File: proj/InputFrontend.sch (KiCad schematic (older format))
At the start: 0 parts

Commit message: Add frontend
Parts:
- added C?: 47u, IPC7351-Nominal:CAPC3216X70, symbol C-1206
- added C? (x12): 1n, IPC7351-Nominal:CAPC1005X55, symbol C-0402
- added C? (x6): 220n, IPC7351-Nominal:CAPC2012X70, symbol C-0805
- added MP?: SHIELD, symbol SHIELD
- added R? (x2): 49R9, IPC7351-Nominal:RESC1005X40, symbol R-0402
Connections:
- new net: C?.1, C?.1, R?.1, R?.2
- new net +5: C?.1, C?.1, C?.1, C?.1, C?.1, C?.1, C?.1, C?.1
- new net -5: C?.1, C?.1, C?.1, C?.1, C?.1, C?.1, C?.1, C?.1, C?.1
- new net Detector/OUT: R?.2
- new net GND: C?.2, C?.2, C?.2, C?.2, C?.2, C?.2, C?.2, C?.2, C?.2, C?.2, C?.2, C?.2, C?.2, C?.2, C?.2, C?.2, C?.2, C?.2, C?.2, MP?.1
- new net OUT: R?.1

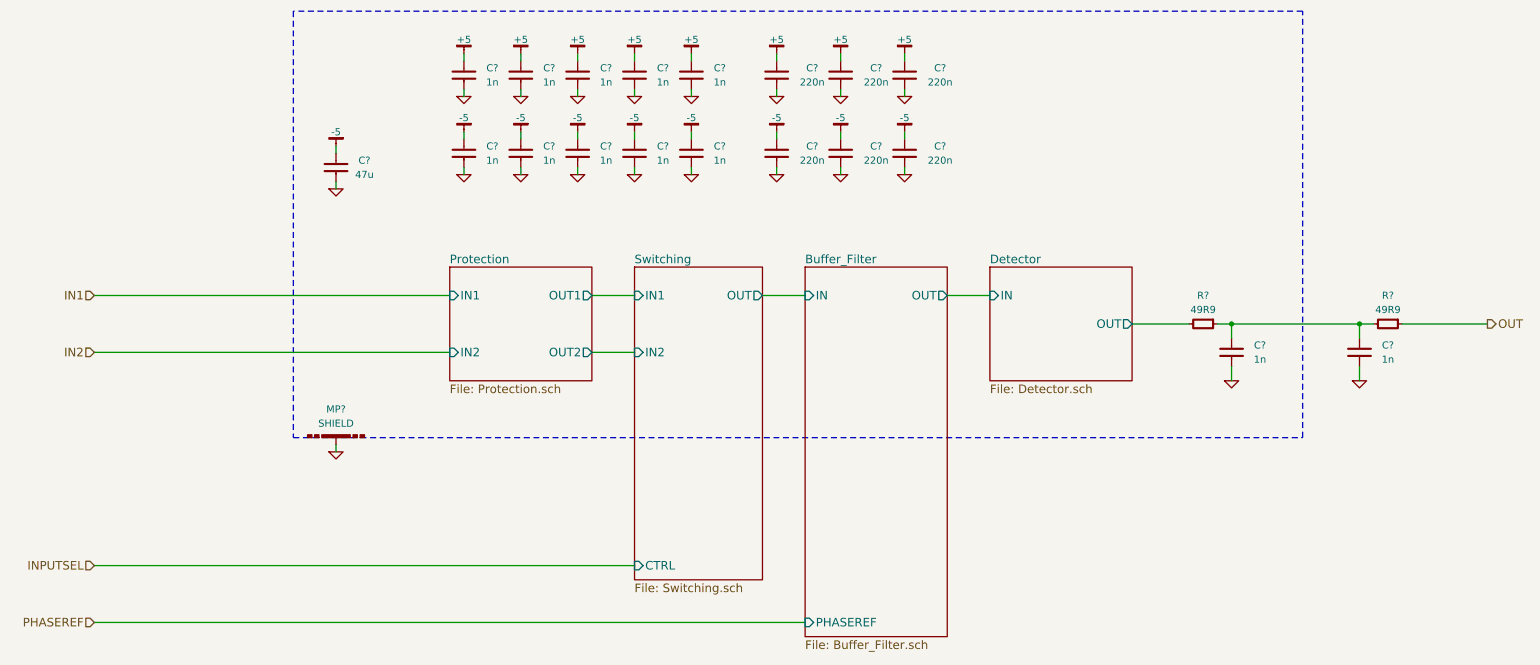
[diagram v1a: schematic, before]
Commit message: Add power input circuit
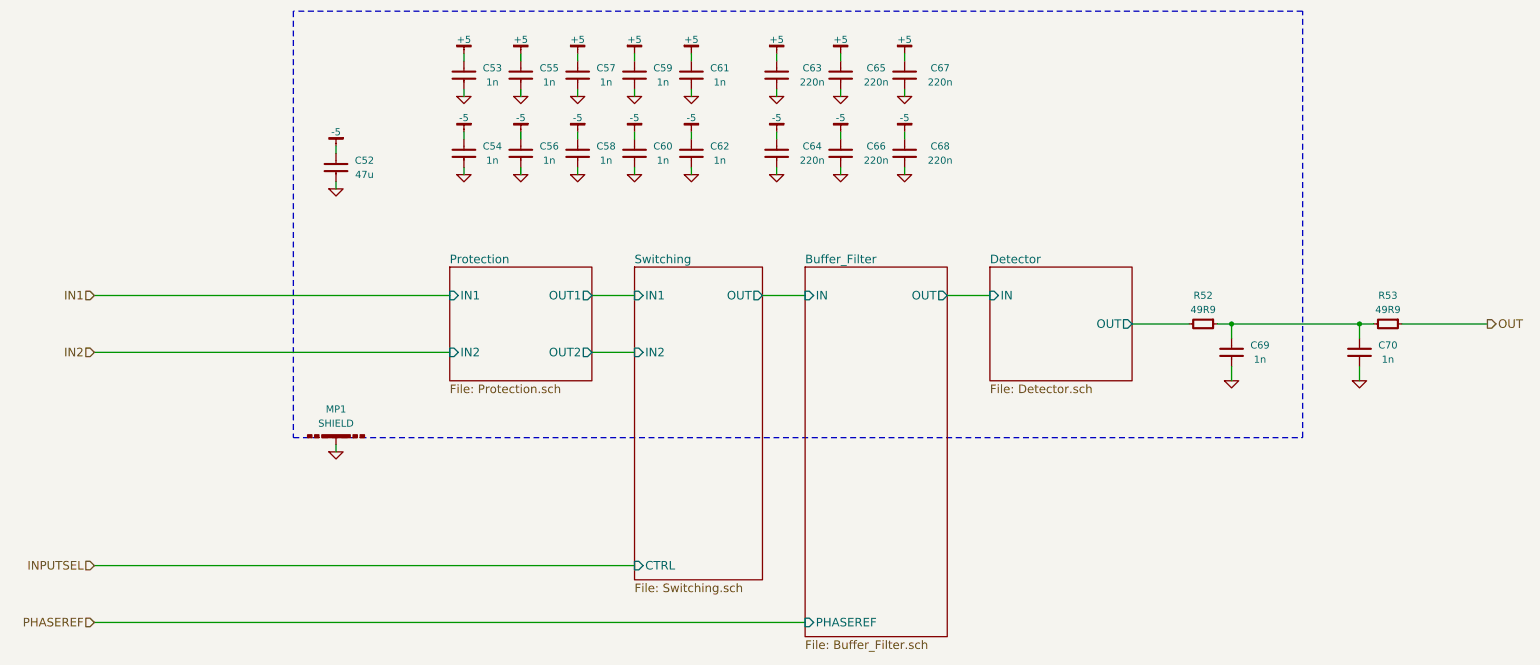
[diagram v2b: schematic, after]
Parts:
- gave numbers to parts that had none: 22

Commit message: Layout most analog bits
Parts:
- MP1: footprint (none) -> manuf:LAIRD-BMI-S-203
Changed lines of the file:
@@
 F 0 "MP1" H 3500 4400 50  0000 C CNN
 F 1 "SHIELD" H 3500 4300 50  0000 C CNN
-F 2 "" H 3500 4200 50  0001 C CNN
+F 2 "manuf:LAIRD-BMI-S-203" H 3500 4200 50  0001 C CNN
 F 3 "" H 3500 4200 50  0000 C CNN
 F 4 "BMI-S-203F; BMI-S-203-C" H 3500 4200 60  0001 C CNN "PN"
@@
 $EndComp
 $Comp
-L GND #PWR0161
+L GND #PWR0162
 U 1 1 54F2F4A0
 P 3500 4300
-F 0 "#PWR0161" H 3500 4300 30  0001 C CNN
+F 0 "#PWR0162" H 3500 4300 30  0001 C CNN
 F 1 "GND" H 3500 4230 30  0001 C CNN
 F 2 "" H 3500 4300 60  0000 C CNN
@@
 	11600 3400 11000 3400
 $Comp
-L GND #PWR0162
+L GND #PWR0163
 U 1 1 54F3075A
 P 9800 3800
-F 0 "#PWR0162" H 9800 3800 30  0001 C CNN
+F 0 "#PWR0163" H 9800 3800 30  0001 C CNN
 F 1 "GND" H 9800 3730 30  0001 C CNN
 F 2 "" H 9800 3800 60  0000 C CNN
@@
 	9800 3700 9800 3800
 $Comp
-L GND #PWR0163
+L GND #PWR0164
 U 1 1 54F3079D
 P 10700 3800
-F 0 "#PWR0163" H 10700 3800 30  0001 C CNN
+F 0 "#PWR0164" H 10700 3800 30  0001 C CNN
 F 1 "GND" H 10700 3730 30  0001 C CNN
 F 2 "" H 10700 3800 60  0000 C CNN
@@
 $EndComp
 $Comp
-L -5 #PWR0164
+L -5 #PWR0165
 U 1 1 54F26D5C
 P 3500 2150
-F 0 "#PWR0164" H 3500 2100 30  0001 C CNN
+F 0 "#PWR0165" H 3500 2100 30  0001 C CNN
 F 1 "-5" H 3500 2050 50  0000 C CNN
 F 2 "" H 3500 2150 60  0000 C CNN
@@
 	3500 2150 3500 2200
 $Comp
-L GND #PWR0165
+L GND #PWR0166
 U 1 1 54F26E11
 P 3500 2450
-F 0 "#PWR0165" H 3500 2450 30  0001 C CNN
+F 0 "#PWR0166" H 3500 2450 30  0001 C CNN
 F 1 "GND" H 3500 2380 30  0001 C CNN
 F 2 "" H 3500 2450 60  0000 C CNN
@@
 $EndComp
 $Comp
-L -5 #PWR0166
+L -5 #PWR0167
 U 1 1 54F284A2
 P 4400 2050
-F 0 "#PWR0166" H 4400 2000 30  0001 C CNN
+F 0 "#PWR0167" H 4400 2000 30  0001 C CNN
 F 1 "-5" H 4400 1950 50  0000 C CNN
 F 2 "" H 4400 2050 60  0000 C CNN
@@
 	4400 2050 4400 2100
 $Comp
-L GND #PWR0167
+L GND #PWR0168
 U 1 1 54F285D9
 P 4400 2350
-F 0 "#PWR0167" H 4400 2350 30  0001 C CNN
+F 0 "#PWR0168" H 4400 2350 30  0001 C CNN
 F 1 "GND" H 4400 2280 30  0001 C CNN
 F 2 "" H 4400 2350 60  0000 C CNN
@@
 $EndComp
 $Comp
-L -5 #PWR0168
+L -5 #PWR0169
 U 1 1 54F286B0
 P 4800 2050
-F 0 "#PWR0168" H 4800 2000 30  0001 C CNN
+F 0 "#PWR0169" H 4800 2000 30  0001 C CNN
 F 1 "-5" H 4800 1950 50  0000 C CNN
 F 2 "" H 4800 2050 60  0000 C CNN
@@
 	4800 2050 4800 2100
 $Comp
-L GND #PWR0169
+L GND #PWR0170
 U 1 1 54F286B7
 P 4800 2350
-F 0 "#PWR0169" H 4800 2350 30  0001 C CNN
+F 0 "#PWR0170" H 4800 2350 30  0001 C CNN
 F 1 "GND" H 4800 2280 30  0001 C CNN
 F 2 "" H 4800 2350 60  0000 C CNN
@@
 $EndComp
 $Comp
-L -5 #PWR0170
+L -5 #PWR0171
 U 1 1 54F2877F
 P 5200 2050
-F 0 "#PWR0170" H 5200 2000 30  0001 C CNN
+F 0 "#PWR0171" H 5200 2000 30  0001 C CNN
 F 1 "-5" H 5200 1950 50  0000 C CNN
 F 2 "" H 5200 2050 60  0000 C CNN
@@
 	5200 2050 5200 2100
 $Comp
-L GND #PWR0171
+L GND #PWR0172
 U 1 1 54F28786
 P 5200 2350
-F 0 "#PWR0171" H 5200 2350 30  0001 C CNN
+F 0 "#PWR0172" H 5200 2350 30  0001 C CNN
 F 1 "GND" H 5200 2280 30  0001 C CNN
 F 2 "" H 5200 2350 60  0000 C CNN
@@
 $EndComp
 $Comp
-L -5 #PWR0172
+L -5 #PWR0173
 U 1 1 54F28795
 P 5600 2050
-F 0 "#PWR0172" H 5600 2000 30  0001 C CNN
+F 0 "#PWR0173" H 5600 2000 30  0001 C CNN
 F 1 "-5" H 5600 1950 50  0000 C CNN
 F 2 "" H 5600 2050 60  0000 C CNN
@@
 	5600 2050 5600 2100
 $Comp
-L GND #PWR0173
+L GND #PWR0174
 U 1 1 54F2879C
 P 5600 2350
-F 0 "#PWR0173" H 5600 2350 30  0001 C CNN
+F 0 "#PWR0174" H 5600 2350 30  0001 C CNN
 F 1 "GND" H 5600 2280 30  0001 C CNN
 F 2 "" H 5600 2350 60  0000 C CNN
@@
 $EndComp
 $Comp
-L -5 #PWR0174
+L -5 #PWR0175
 U 1 1 54F2882B
 P 6000 2050
-F 0 "#PWR0174" H 6000 2000 30  0001 C CNN
+F 0 "#PWR0175" H 6000 2000 30  0001 C CNN
 F 1 "-5" H 6000 1950 50  0000 C CNN
 F 2 "" H 6000 2050 60  0000 C CNN
@@
 	6000 2050 6000 2100
 $Comp
-L GND #PWR0175
+L GND #PWR0176
 U 1 1 54F28832
 P 6000 2350
-F 0 "#PWR0175" H 6000 2350 30  0001 C CNN
+F 0 "#PWR0176" H 6000 2350 30  0001 C CNN
 F 1 "GND" H 6000 2280 30  0001 C CNN
 F 2 "" H 6000 2350 60  0000 C CNN
@@
 	4400 1500 4400 1550
 $Comp
-L GND #PWR0176
+L GND #PWR0177
 U 1 1 54F288BE
 P 4400 1800
-F 0 "#PWR0176" H 4400 1800 30  0001 C CNN
+F 0 "#PWR0177" H 4400 1800 30  0001 C CNN
 F 1 "GND" H 4400 1730 30  0001 C CNN
 F 2 "" H 4400 1800 60  0000 C CNN
@@
 	4400 1800 4400 1750
 $Comp
-L +5 #PWR0177
+L +5 #PWR0178
 U 1 1 54F2892E
 P 4400 1500
-F 0 "#PWR0177" H 4400 1550 30  0001 C CNN
+F 0 "#PWR0178" H 4400 1550 30  0001 C CNN
 F 1 "+5" H 4400 1600 50  0000 C CNN
 F 2 "" H 4400 1500 60  0000 C CNN
@@
 	4800 1500 4800 1550
 $Comp
-L GND #PWR0178
+L GND #PWR0179
 U 1 1 54F28A98
 P 4800 1800
-F 0 "#PWR0178" H 4800 1800 30  0001 C CNN
+F 0 "#PWR0179" H 4800 1800 30  0001 C CNN
 F 1 "GND" H 4800 1730 30  0001 C CNN
 F 2 "" H 4800 1800 60  0000 C CNN
@@
 	4800 1800 4800 1750
 $Comp
-L +5 #PWR0179
+L +5 #PWR0180
 U 1 1 54F28A9F
 P 4800 1500
-F 0 "#PWR0179" H 4800 1550 30  0001 C CNN
+F 0 "#PWR0180" H 4800 1550 30  0001 C CNN
 F 1 "+5" H 4800 1600 50  0000 C CNN
 F 2 "" H 4800 1500 60  0000 C CNN
@@
 	5200 1500 5200 1550
 $Comp
-L GND #PWR0180
+L GND #PWR0181
 U 1 1 54F28B62
 P 5200 1800
-F 0 "#PWR0180" H 5200 1800 30  0001 C CNN
+F 0 "#PWR0181" H 5200 1800 30  0001 C CNN
 F 1 "GND" H 5200 1730 30  0001 C CNN
 F 2 "" H 5200 1800 60  0000 C CNN
@@
 	5200 1800 5200 1750
 $Comp
-L +5 #PWR0181
+L +5 #PWR0182
 U 1 1 54F28B69
 P 5200 1500
-F 0 "#PWR0181" H 5200 1550 30  0001 C CNN
+F 0 "#PWR0182" H 5200 1550 30  0001 C CNN
 F 1 "+5" H 5200 1600 50  0000 C CNN
 F 2 "" H 5200 1500 60  0000 C CNN
@@
 	5600 1500 5600 1550
 $Comp
-L GND #PWR0182
+L GND #PWR0183
 U 1 1 54F28B78
 P 5600 1800
-F 0 "#PWR0182" H 5600 1800 30  0001 C CNN
+F 0 "#PWR0183" H 5600 1800 30  0001 C CNN
 F 1 "GND" H 5600 1730 30  0001 C CNN
 F 2 "" H 5600 1800 60  0000 C CNN
@@
 	5600 1800 5600 1750
 $Comp
-L +5 #PWR0183
+L +5 #PWR0184
 U 1 1 54F28B7F
 P 5600 1500
-F 0 "#PWR0183" H 5600 1550 30  0001 C CNN
+F 0 "#PWR0184" H 5600 1550 30  0001 C CNN
 F 1 "+5" H 5600 1600 50  0000 C CNN
 F 2 "" H 5600 1500 60  0000 C CNN
@@
 	6000 1500 6000 1550
 $Comp
-L GND #PWR0184
+L GND #PWR0185
 U 1 1 54F28CBF
 P 6000 1800
-F 0 "#PWR0184" H 6000 1800 30  0001 C CNN
+F 0 "#PWR0185" H 6000 1800 30  0001 C CNN
 F 1 "GND" H 6000 1730 30  0001 C CNN
 F 2 "" H 6000 1800 60  0000 C CNN
@@
 	6000 1800 6000 1750
 $Comp
-L +5 #PWR0185
+L +5 #PWR0186
 U 1 1 54F28CC6
 P 6000 1500
-F 0 "#PWR0185" H 6000 1550 30  0001 C CNN
+F 0 "#PWR0186" H 6000 1550 30  0001 C CNN
 F 1 "+5" H 6000 1600 50  0000 C CNN
 F 2 "" H 6000 1500 60  0000 C CNN
@@
 $EndComp
 $Comp
-L -5 #PWR0186
+L -5 #PWR0187
 U 1 1 54F29712
 P 6600 2050
-F 0 "#PWR0186" H 6600 2000 30  0001 C CNN
+F 0 "#PWR0187" H 6600 2000 30  0001 C CNN
 F 1 "-5" H 6600 1950 50  0000 C CNN
 F 2 "" H 6600 2050 60  0000 C CNN
@@
 	6600 2050 6600 2100
 $Comp
-L GND #PWR0187
+L GND #PWR0188
 U 1 1 54F297C4
 P 6600 2350
-F 0 "#PWR0187" H 6600 2350 30  0001 C CNN
+F 0 "#PWR0188" H 6600 2350 30  0001 C CNN
 F 1 "GND" H 6600 2280 30  0001 C CNN
 F 2 "" H 6600 2350 60  0000 C CNN
@@
 $EndComp
 $Comp
-L -5 #PWR0188
+L -5 #PWR0189
 U 1 1 54F298CF
 P 7050 2050
-F 0 "#PWR0188" H 7050 2000 30  0001 C CNN
+F 0 "#PWR0189" H 7050 2000 30  0001 C CNN
 F 1 "-5" H 7050 1950 50  0000 C CNN
 F 2 "" H 7050 2050 60  0000 C CNN
@@
 	7050 2050 7050 2100
 $Comp
-L GND #PWR0189
+L GND #PWR0190
 U 1 1 54F298D6
 P 7050 2350
-F 0 "#PWR0189" H 7050 2350 30  0001 C CNN
+F 0 "#PWR0190" H 7050 2350 30  0001 C CNN
 F 1 "GND" H 7050 2280 30  0001 C CNN
 F 2 "" H 7050 2350 60  0000 C CNN
@@
 $EndComp
 $Comp
-L -5 #PWR0190
+L -5 #PWR0191
 U 1 1 54F299AC
 P 7500 2050
-F 0 "#PWR0190" H 7500 2000 30  0001 C CNN
+F 0 "#PWR0191" H 7500 2000 30  0001 C CNN
 F 1 "-5" H 7500 1950 50  0000 C CNN
 F 2 "" H 7500 2050 60  0000 C CNN
@@
 	7500 2050 7500 2100
 $Comp
-L GND #PWR0191
+L GND #PWR0192
 U 1 1 54F299B3
 P 7500 2350
-F 0 "#PWR0191" H 7500 2350 30  0001 C CNN
+F 0 "#PWR0192" H 7500 2350 30  0001 C CNN
 F 1 "GND" H 7500 2280 30  0001 C CNN
 F 2 "" H 7500 2350 60  0000 C CNN
@@
 	6600 1500 6600 1550
 $Comp
-L GND #PWR0192
+L GND #PWR0193
 U 1 1 54F29AAD
 P 6600 1800
-F 0 "#PWR0192" H 6600 1800 30  0001 C CNN
+F 0 "#PWR0193" H 6600 1800 30  0001 C CNN
 F 1 "GND" H 6600 1730 30  0001 C CNN
 F 2 "" H 6600 1800 60  0000 C CNN
@@
 	6600 1800 6600 1750
 $Comp
-L +5 #PWR0193
+L +5 #PWR0194
 U 1 1 54F29B68
 P 6600 1500
-F 0 "#PWR0193" H 6600 1550 30  0001 C CNN
+F 0 "#PWR0194" H 6600 1550 30  0001 C CNN
 F 1 "+5" H 6600 1600 50  0000 C CNN
 F 2 "" H 6600 1500 60  0000 C CNN
@@
 	7050 1500 7050 1550
 $Comp
-L GND #PWR0194
+L GND #PWR0195
 U 1 1 54F29C50
 P 7050 1800
-F 0 "#PWR0194" H 7050 1800 30  0001 C CNN
+F 0 "#PWR0195" H 7050 1800 30  0001 C CNN
 F 1 "GND" H 7050 1730 30  0001 C CNN
 F 2 "" H 7050 1800 60  0000 C CNN
@@
 	7050 1800 7050 1750
 $Comp
-L +5 #PWR0195
+L +5 #PWR0196
 U 1 1 54F29C57
 P 7050 1500
-F 0 "#PWR0195" H 7050 1550 30  0001 C CNN
+F 0 "#PWR0196" H 7050 1550 30  0001 C CNN
 F 1 "+5" H 7050 1600 50  0000 C CNN
 F 2 "" H 7050 1500 60  0000 C CNN
@@
 	7500 1500 7500 1550
 $Comp
-L GND #PWR0196
+L GND #PWR0197
 U 1 1 54F29CFE
 P 7500 1800
-F 0 "#PWR0196" H 7500 1800 30  0001 C CNN
+F 0 "#PWR0197" H 7500 1800 30  0001 C CNN
 F 1 "GND" H 7500 1730 30  0001 C CNN
 F 2 "" H 7500 1800 60  0000 C CNN
@@
 	7500 1800 7500 1750
 $Comp
-L +5 #PWR0197
+L +5 #PWR0198
 U 1 1 54F29D05
 P 7500 1500
-F 0 "#PWR0197" H 7500 1550 30  0001 C CNN
+F 0 "#PWR0198" H 7500 1550 30  0001 C CNN
 F 1 "+5" H 7500 1600 50  0000 C CNN
 F 2 "" H 7500 1500 60  0000 C CNN
